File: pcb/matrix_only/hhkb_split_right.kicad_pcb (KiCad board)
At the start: 2 copper layers, 173.7 x 97.4 mm, 83 parts, among them SW1 CPG151101S11-2, SW10 CPG151101S11-2, SW11 CPG151101S11-2, SW12 CPG151101S11-2, SW13 CPG151101S11-2, SW14 CPG151101S11-2, SW15 CPG151101S11-2, SW16 CPG151101S11-2, SW17 CPG151101S11-2, SW18 CPG151101S11-2, SW19 CPG151101S11-2, SW2 CPG151101S11-2, SW20 CPG151101S11-2, SW21 CPG151101S11-2, SW22 CPG151101S11-2, SW23 CPG151101S11-2, SW24 CPG151101S11-2, SW25 CPG151101S11-2, SW26 CPG151101S11-2, SW27 CPG151101S11-2, SW28 CPG151101S11-2, SW29 CPG151101S11-2, SW3 CPG151101S11-2, SW30 CPG151101S11-2, SW31 CPG151101S11-2, SW32 CPG151101S11-2, SW33 CPG151101S11-2, SW34 CPG151101S11-2, SW4 CPG151101S11-2, SW5 CPG151101S11-2, SW6 CPG151101S11-2, SW7 CPG151101S11-2, SW8 CPG151101S11-2, SW9 CPG151101S11-2, U1 74LVC595, U2 74LVC595

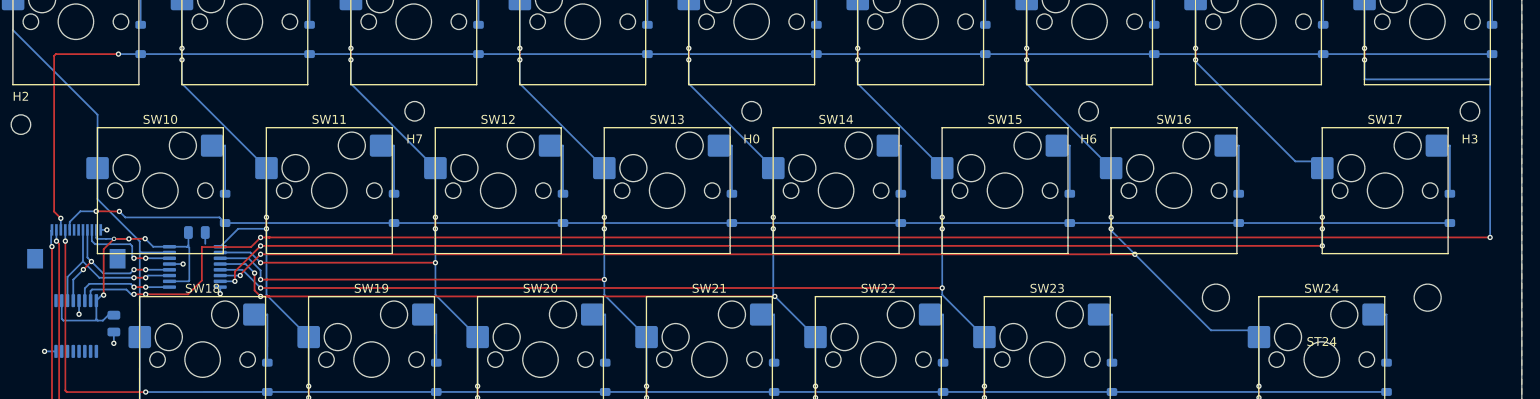
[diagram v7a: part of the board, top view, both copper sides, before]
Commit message: 両手とも決定的な配置配線が揃った（左右ともエラー 0・未配線 0）
利用者「これで一旦、決定的な配置配線は、右手に限り完了した」
「このノウハウを、左手に展開してください」→ 展開 → 利用者が左右とも仕上げ。

    左  エラー 0 / 未配線 0   配線 279 区間・ビア 62・GND 4+スタブ 5
    右  エラー 0 / 未配線 0   配線 349 区間・ビア 87・GND 7+スタブ 8

## 左へ展開したこと

**取付穴 H0 を帯の外へ。**(2.50, 9.00) → **(2.50, -9.00)**。
⚠️ **右と同じ答えにはならなかった。**右は「y=28 の既存の列に載せる」が
正解だったが、**左は穴が 6 本しか無く H0 が中央の支えを兼ねている。**
y=28 へ動かすと**キーからの最大距離が 34.36 → 47.05mm** に悪化する。
**x はそのまま y を符号反転**（帯の反対側）で **34.36 → 31.01mm**。
**手順は同じでも答えは測って出す。**

**横ライン 6 本。**間隔 0.95mm 均一・右端 189.000 統一・完全な降順。
⚠️ **右は昇順、左は降順。**U1 のパッドが左は上から COL5→COL1 だから
（鏡像なので逆になる）。扇形の開きは最大 0.600mm（右は 1.700mm）。

## 利用者が仕上げたこと

**左**: 扇形 6 本・ROW 5 本・V3V3/SPI/CS/SPARE を全部接続（+93 区間）。
C_U1 を U1 の上へ寄せた（板 201.950,91.000 → 201.070,86.500）。
**J_DB 手前の詰まりを、ビアを階段状に散らして解いた**——
私が「どの径でも成立しない」と言った ROW_D が **0.150 → 0.319mm**。
**径ではなく位置で解くのが正解だった。**ビアも全部 φ0.6 に統一。

**右**: **レーン左端の余分なビア 7 個を削除。**私が置いたもので、
**両側が F.Cu ＝ 層をまたがないので意味が無い**（`via_dangling` 7→2）。
SPARE/SPARE2 を J_DB へ接続。

## スクリプト側

`export_matrix_routing.py`
  * **GND のビアとスタブも写す。**利用者が V3V3 から離した位置
    （0.302/0.312mm → 1.26〜1.86mm）が、次の生成で消えていた。
    ⚠️ **「電源から N mm 離す」という規則にして失敗した**——候補を弾くと
    逆に V3V3 の**配線**側へ押し出され、7 個中 4 個が落ちて U1/U2 の
    GND パッドがベタに繋がらなくなった。`gnd_fanout.py` は元へ戻した。
    **パッドしか見ない探索に、配線の都合は表現できない。現物を写す。**
  * **アニュラー不足のビアを規格まで広げる。**KiCad の既定ビアは
    φ0.5/穴 0.3 でアニュラー 0.100mm、JLC の下限は 0.130mm。
    **手で引くと必ず踏む**（実測 左 10・右 1）。穴は変えない。
    ⚠️ **標準の φ0.6 へ揃えたら `clearance` が 2 件出た。**詰まった場所は
    太らせる余地が無い。**規格を満たす最小に留める。**

`gen_pcb.py`
  * `apply_matrix_routing` が GND のビアとスタブも載せる。
  * `_drop_gnd_vias_hitting` が**スタブの線も落とす**。ビアだけ消すと
    線が残り、あとから載る配線と `tracks_crossing` になった。

`pcb_rules.py`  DECOUPLE_OFFSET["left"]["C_U1"] を利用者の位置へ。

## 一致を数えた

    left  GND 以外 341/341  GND  9/9    差 0（SPARE 2 本が 0.001mm の丸め）
    right GND 以外 436/436  GND 15/15   差 0

## 直した取りこぼし

**COL の斜め線が編集中に消えていた**（縦バス下端 → 下の行）。
右 4 本・左 5 本。元の座標のまま戻した。`ROW_A` の孤児 1 本は削除。

⚠️ `isolated_copper`（左 47・右 62）は**縫いビアを既定で打たない設定**
（利用者「それは最後にやる工程」）。`GND_STIT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
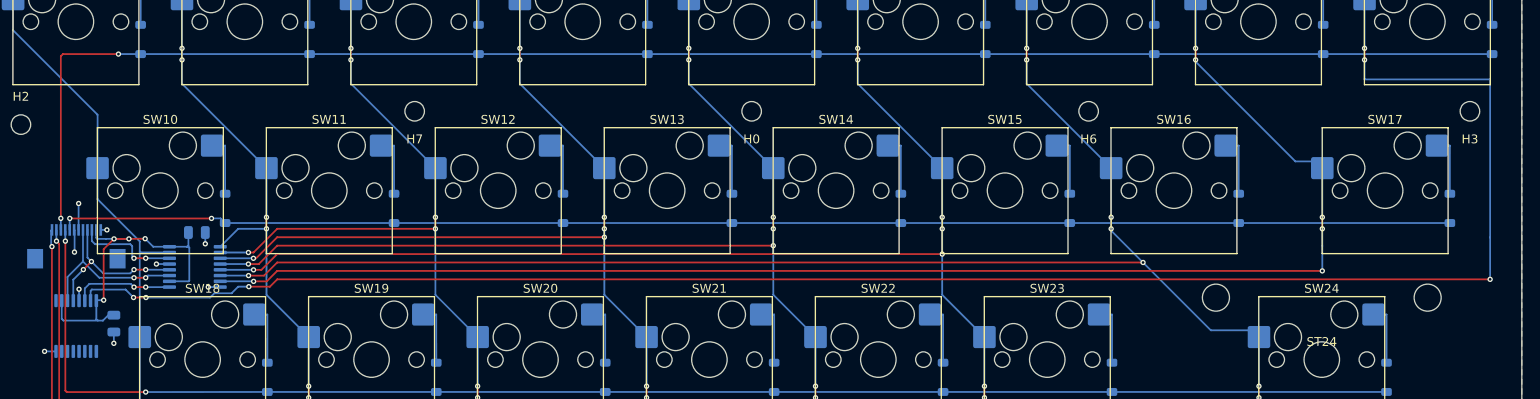
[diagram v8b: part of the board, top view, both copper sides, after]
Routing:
- net SPARE2: track 0.00 -> 2.98 mm, vias 0 -> 1
- net SPARE: track 0.00 -> 2.53 mm, vias 0 -> 1
- net COL4: track 153.5 -> 151.3 mm, vias 11 -> 10
- net ROW_C: track 182.2 -> 181.1 mm
- net COL7: track 162.1 -> 163.1 mm, vias 7 -> 6
- net COL3: track 131.1 -> 130.4 mm
- net COL2: track 91.8 -> 92.4 mm, vias 8 -> 7
- net ROW_A: track 157.7 -> 157.1 mm
- net COL6: track 180.3 -> 180.8 mm, vias 9 -> 8
- net GND: track 8.36 -> 8.65 mm, vias 6 -> 7
